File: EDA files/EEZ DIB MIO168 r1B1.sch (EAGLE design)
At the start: 295 parts, among them IC1 M24C32-WMN6P, IC10 DAC7760IPWPR, IC11 DAC7760IPWPR, IC12 OPA376AIDBVR, IC13 DAC7563TDGSR, IC14 OPA2196IDR, IC15 BTS3408G, IC16 BTS3408G, IC17 BTS3408G, IC18 BTS3408G, IC19 74HC126PW,118, IC2 Si8641BB-B-IS1, IC20 TL431B, IC21 DG468DV-T1-E3, IC22 DG468DV-T1-E3, IC23 DG468DV-T1-E3, IC24 DG468DV-T1-E3, IC25 DG468DV-T1-E3, IC26 DG468DV-T1-E3, IC27 DG468DV-T1-E3, IC28 DG468DV-T1-E3, IC29 DG468DV-T1-E3, IC3 Si8641BB-B-IS1, IC30 DG468DV-T1-E3, IC31 DG468DV-T1-E3, IC32 DG468DV-T1-E3, IC33 DG468DV-T1-E3, IC34 DG468DV-T1-E3, IC35 OPA376AIDBVR, IC36 ADS8674IDBT, IC4 L78L12, IC5 LP2985-50DBVR, IC6 LP2985-33DBVR, IC7 L79L12, IC8 STM32F446ZCT6, IC9 OPA2196IDR, J1 4907, J2 503398-1892, Q1 2N7002PS, Q10 BSS169, Q11 BSS169, Q12 BSS169, Q13 BSS169, Q2 2N7002PS, Q3 2N7002PS, Q4 2N7002PS, Q5 2N7002PS, Q6 BSS169, Q7 BSS169, Q8 BSS169, Q9 BSS169, X1 77317-104-28LF, X2 SSW-106-02-S-S, X3 691327310016, X4 691327310016, Y1 25MHz

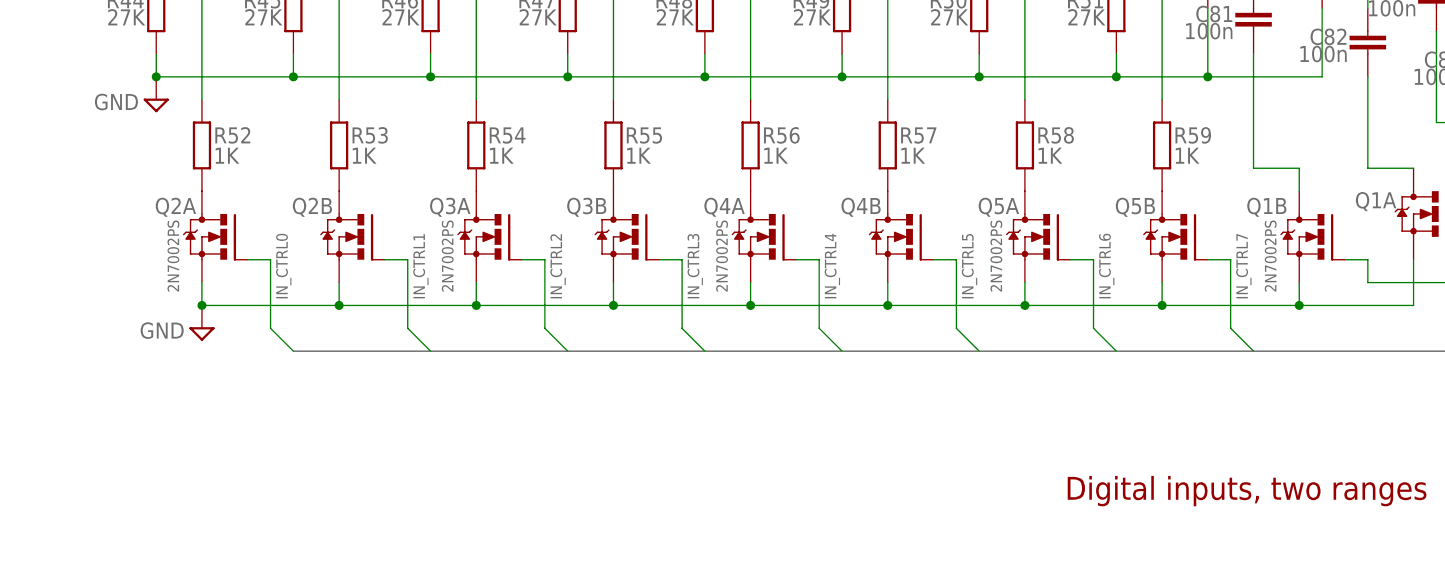
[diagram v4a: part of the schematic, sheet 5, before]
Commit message: 2N7002PS package fixed
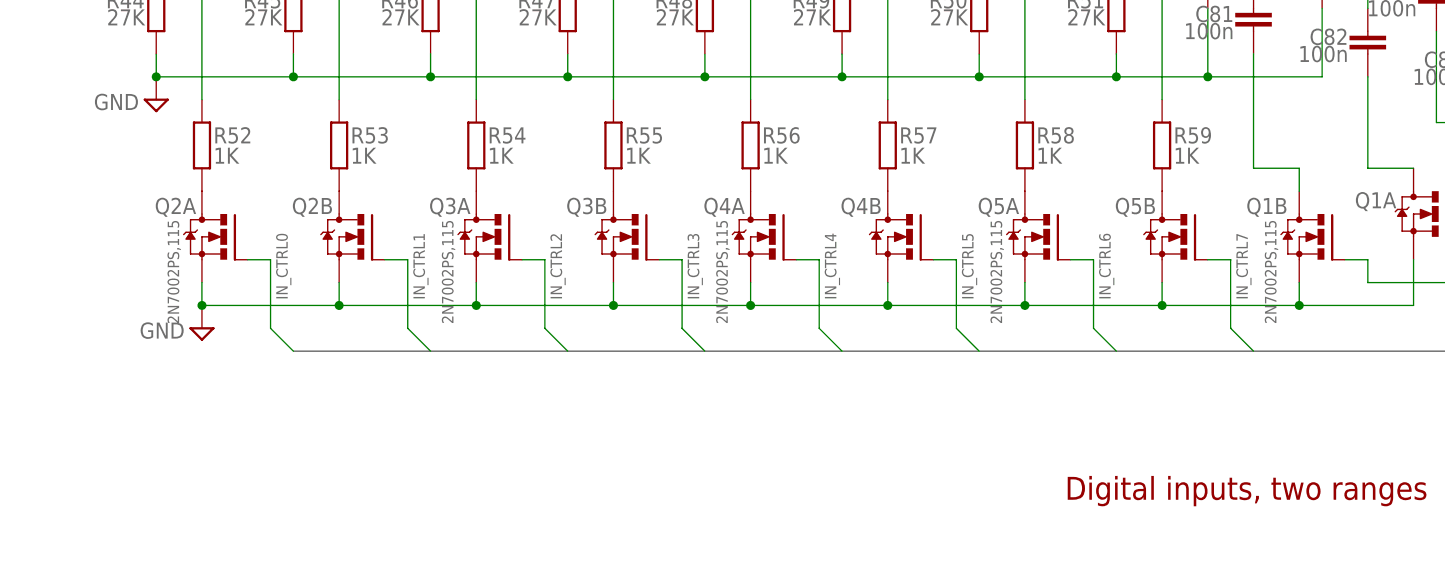
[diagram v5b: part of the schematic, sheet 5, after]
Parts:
- Q1, Q2, Q3, Q4, Q5: value 2N7002PS -> 2N7002PS,115; device EEZ_DIB:2N7002PS -> EEZ_DIB:2N7002PS,115
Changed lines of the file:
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@@
 <setting verticaltext="up"/>
 </settings>
-<grid distance="0.025" unitdist="inch" unit="inch" style="lines" multiple="4" display="no" altdistance="0.01" altunitdist="inch" altunit="inch"/>
+<grid distance="0.1" unitdist="inch" unit="inch" style="lines" multiple="1" display="no" altdistance="0.01" altunitdist="inch" altunit="inch"/>
 <layers>
 <layer number="1" name="Top" color="4" fill="1" visible="no" active="no"/>
@@
 <part name="R50" library="rcl" deviceset="R-EU_" device="R0805" value="27K"/>
 <part name="R51" library="rcl" deviceset="R-EU_" device="R0805" value="27K"/>
-<part name="Q2" library="EEZ_DIB" deviceset="2N7002PS" device=""/>
-<part name="Q3" library="EEZ_DIB" deviceset="2N7002PS" device=""/>
-<part name="Q4" library="EEZ_DIB" deviceset="2N7002PS" device=""/>
-<part name="Q5" library="EEZ_DIB" deviceset="2N7002PS" device=""/>
+<part name="Q2" library="EEZ_DIB" deviceset="2N7002PS" device=",115"/>
+<part name="Q3" library="EEZ_DIB" deviceset="2N7002PS" device=",115"/>
+<part name="Q4" library="EEZ_DIB" deviceset="2N7002PS" device=",115"/>
+<part name="Q5" library="EEZ_DIB" deviceset="2N7002PS" device=",115"/>
 <part name="SUPPLY3" library="supply2" deviceset="GND" device=""/>
 <part name="R52" library="rcl" deviceset="R-EU_" device="R0805" value="1K"/>
@@
 <part name="R58" library="rcl" deviceset="R-EU_" device="R0805" value="1K"/>
 <part name="R59" library="rcl" deviceset="R-EU_" device="R0805" value="1K"/>
-<part name="Q1" library="EEZ_DIB" deviceset="2N7002PS" device=""/>
+<part name="Q1" library="EEZ_DIB" deviceset="2N7002PS" device=",115"/>
 <part name="SUPPLY46" library="supply2" deviceset="GND" device=""/>
 <part name="C81" library="rcl" deviceset="C-EU" device="C0603" value="100n"/>

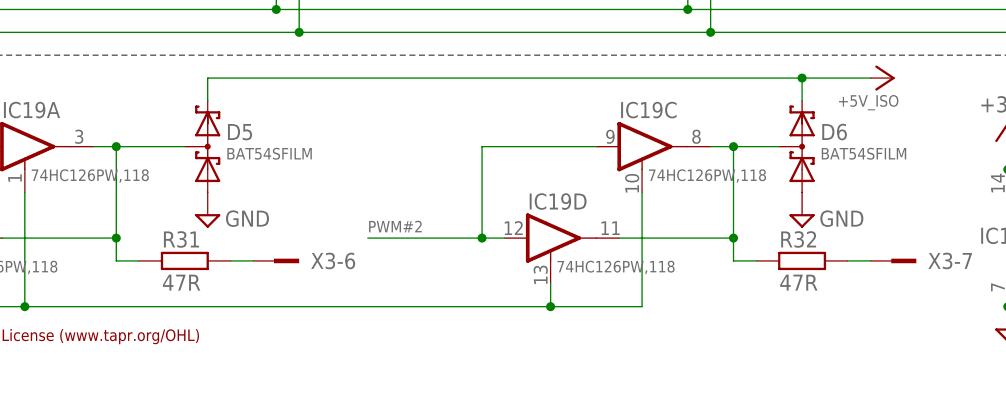
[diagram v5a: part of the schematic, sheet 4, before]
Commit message: front panel connectors position adjusted
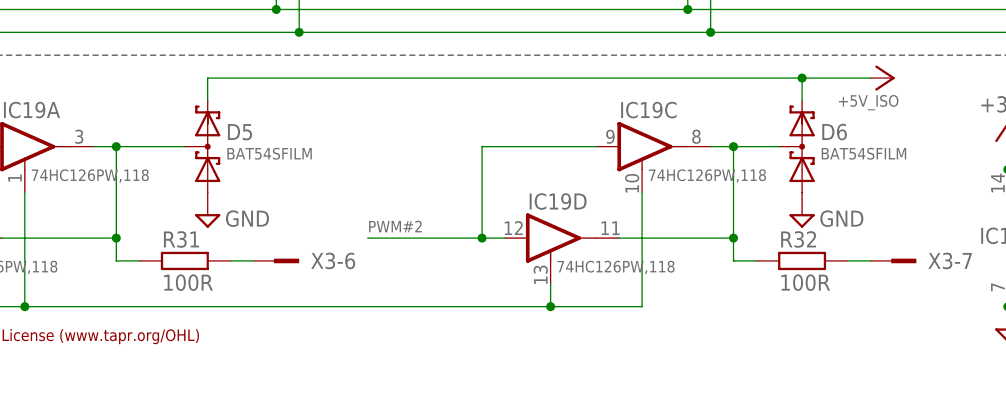
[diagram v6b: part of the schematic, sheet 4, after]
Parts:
- R31, R32: value 47R -> 100R
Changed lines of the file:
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@@
 <part name="U$31" library="EEZ_DIB" deviceset="+5V_ISO" device=""/>
 <part name="JP3" library="EEZ_Lib1" deviceset="JP3-CUT" device=""/>
-<part name="R31" library="rcl" deviceset="R-EU_" device="R0805" value="47R"/>
-<part name="R32" library="rcl" deviceset="R-EU_" device="R0805" value="47R"/>
+<part name="R31" library="rcl" deviceset="R-EU_" device="R0805" value="100R"/>
+<part name="R32" library="rcl" deviceset="R-EU_" device="R0805" value="100R"/>
 <part name="R80" library="rcl" deviceset="R-EU_" device="R1206" value="560K"/>
 <part name="R81" library="rcl" deviceset="R-EU_" device="R1206" value="560K"/>
